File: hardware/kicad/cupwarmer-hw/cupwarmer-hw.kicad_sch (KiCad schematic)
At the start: 6 parts

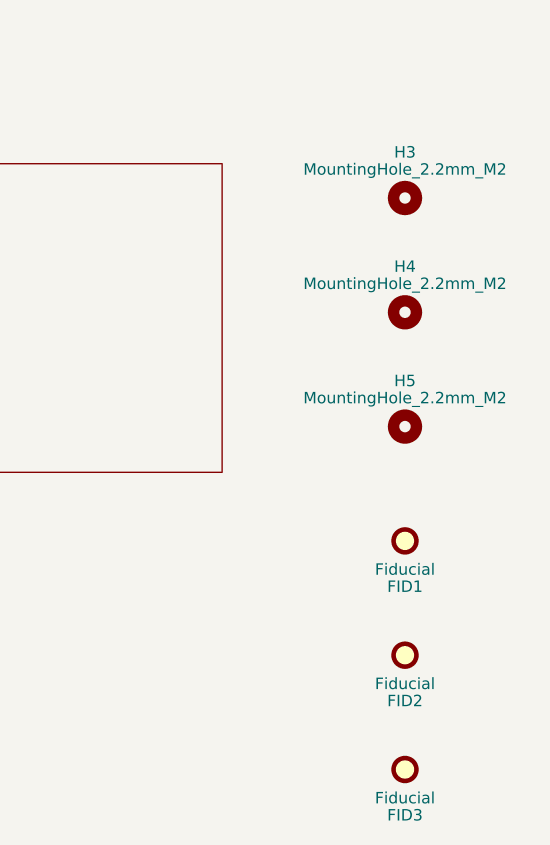
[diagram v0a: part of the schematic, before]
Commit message: Remove PCB mounting holes
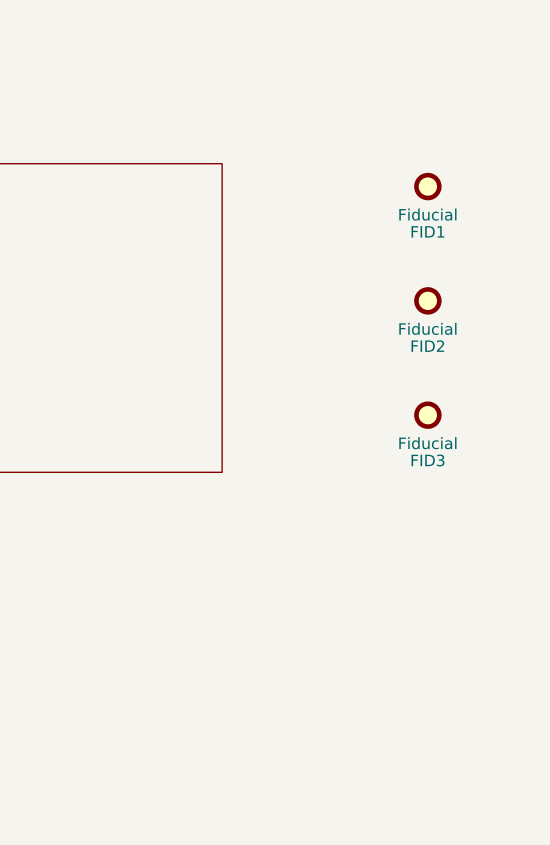
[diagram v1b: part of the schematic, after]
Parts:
- removed H3, H4, H5: MountingHole_2.2mm_M2, MountingHole:MountingHole_2.2mm_M2, symbol Mechanical:MountingHole
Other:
- moved on the sheet: FID1, FID2, FID3
